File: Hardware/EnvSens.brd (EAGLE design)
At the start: 19.4 x 27 mm, 30 parts, among them U1 BME680, U2 LTR-303ALS-01, U3 AB0805-T3, X1 ABS07-120-32.768KHZ-T

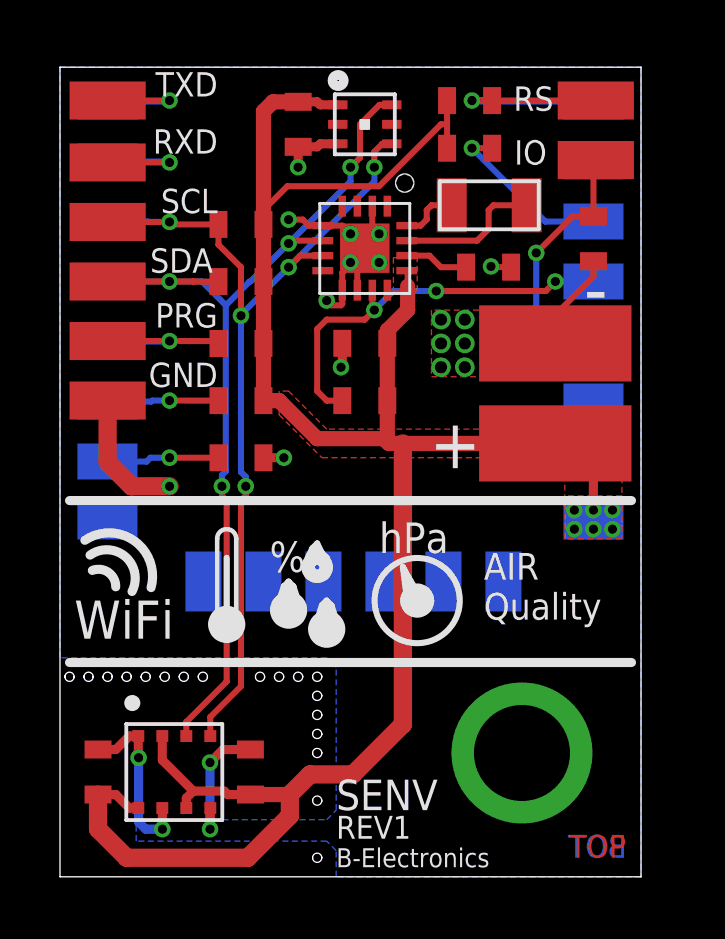
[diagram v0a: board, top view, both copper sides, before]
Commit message: Fix wake up issue
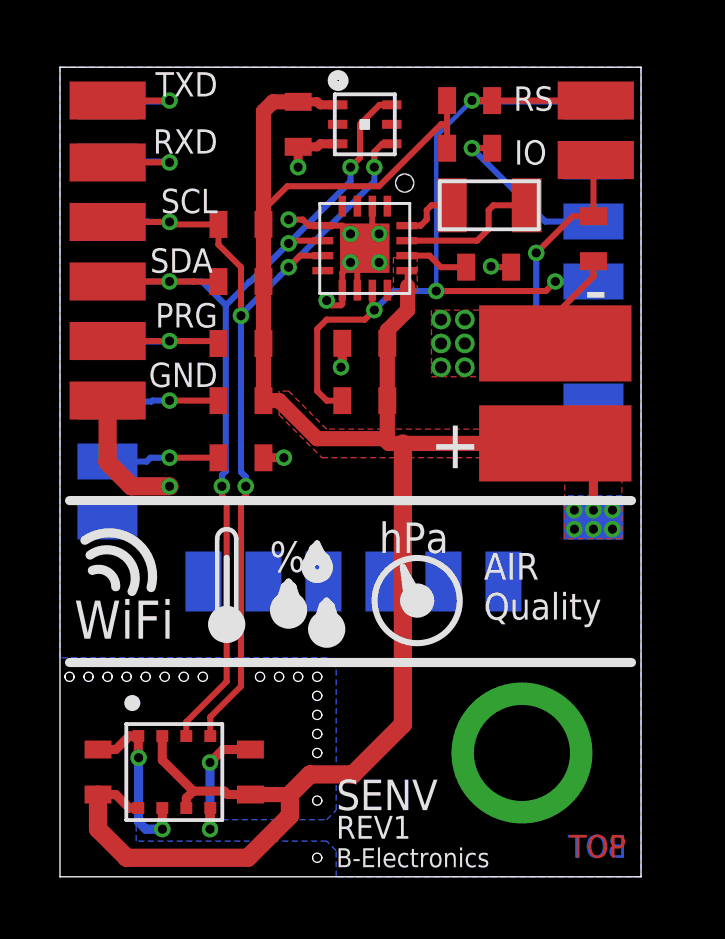
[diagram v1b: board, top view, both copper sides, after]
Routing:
- net WAKE: track 22.5 -> 29.3 mm
